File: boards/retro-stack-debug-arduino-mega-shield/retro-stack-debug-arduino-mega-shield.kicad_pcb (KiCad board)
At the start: 2 copper layers, 90.2 x 53.3 mm, 17 parts, among them J1 Power, J2 PWM, J3 Analog, J4 PWM, J5 Analog, J6 Communication, J7 Digital, J8 BUS_6502

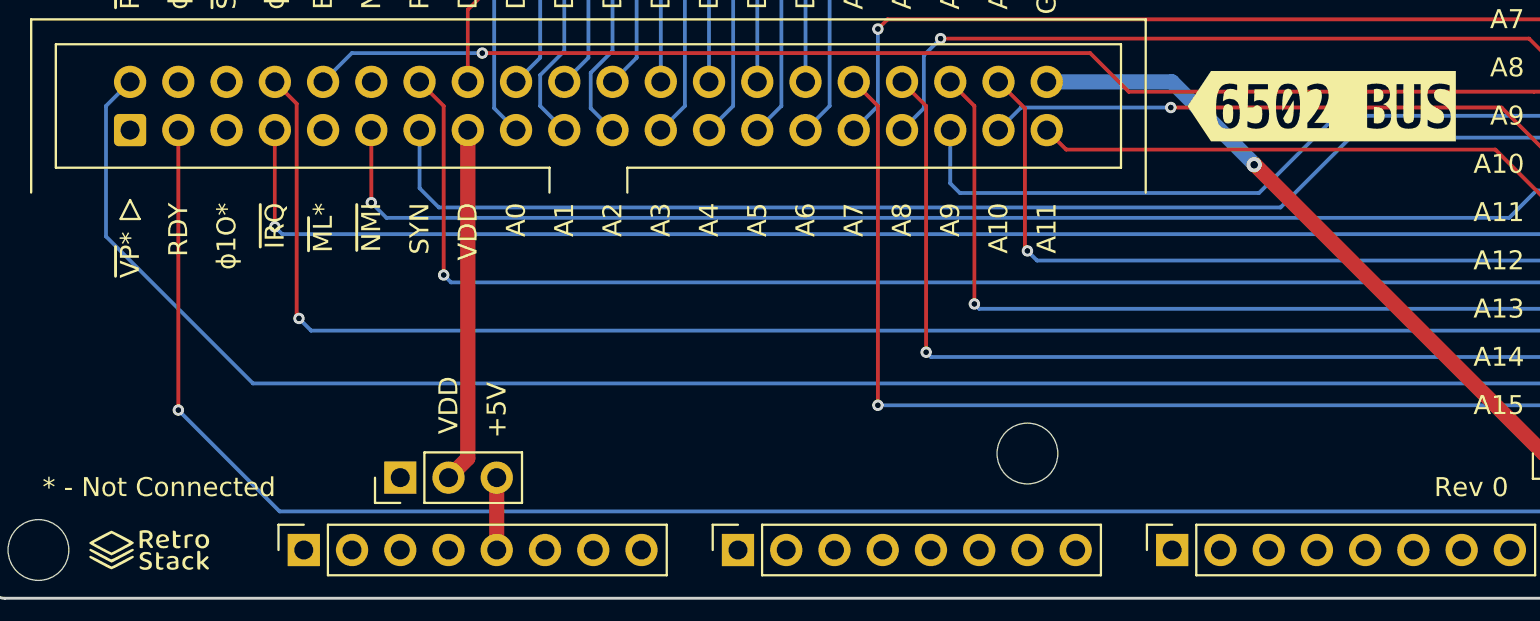
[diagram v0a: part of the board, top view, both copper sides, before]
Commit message: Completed rev 0 of cpu, debug, and debug shield boards.
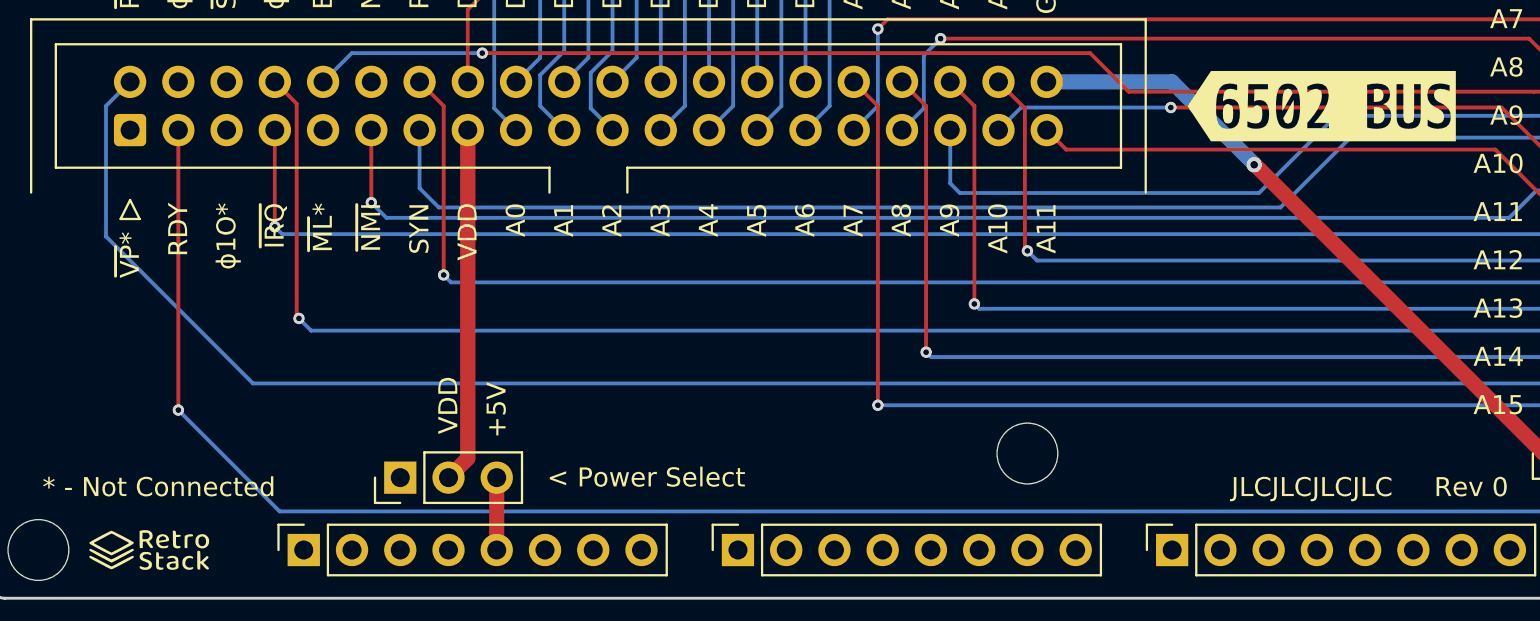
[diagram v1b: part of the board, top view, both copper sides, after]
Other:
- board text added: "< Power Select"
- board text added: "JLCJLCJLCJLC"
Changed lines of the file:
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@@
     (fp_line (start -2.18 -5.1) (end 5.72 -5.1) (layer "F.Fab") (width 0.1))
     (fp_line (start 5.72 -5.1) (end 5.72 53.36) (layer "F.Fab") (width 0.1))
-    (pad "1" thru_hole roundrect (at 0 0 90) (size 1.7 1.7) (drill 1) (layers *.Cu *.Mask) (roundrect_rratio 0.147059)
+    (pad "1" thru_hole roundrect (at 0 0 90) (size 1.7 1.7) (drill 1) (layers *.Cu *.Mask) (roundrect_rratio 0.1470588235)
       (net 79 "/VPB") (pinfunction "Pin_1") (pintype "passive"))
     (pad "2" thru_hole circle (at 2.54 0 90) (size 1.7 1.7) (drill 1) (layers *.Cu *.Mask)
@@
     (effects (font (size 1 1) (thickness 0.153)) (justify left))
   )
+  (gr_text "JLCJLCJLCJLC" (at 181.026 94.158) (layer "F.SilkS")
+    (effects (font (size 1 1) (thickness 0.153)))
+  )
   (gr_text "GND" (at 167.056 69.266 90) (layer "F.SilkS")
     (effects (font (size 1 1) (thickness 0.153)) (justify left))
@@
     (effects (font (size 1 1) (thickness 0.153)) (justify left))
   )
+  (gr_text "< Power Select" (at 145.974 93.65) (layer "F.SilkS")
+    (effects (font (size 1 1) (thickness 0.153)))
+  )
   (gr_text "ϕ2O*" (at 121.336 69.012 90) (layer "F.SilkS")
